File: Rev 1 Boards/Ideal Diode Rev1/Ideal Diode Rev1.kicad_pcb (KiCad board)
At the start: 2 copper layers, 66.8 x 54.6 mm, 21 parts, among them J2 Conn_01x02_Socket, J3 Conn_01x02_Socket, Q1 NVMFS5C404NL, U1 SN74LVC2G08, U2 LM74700

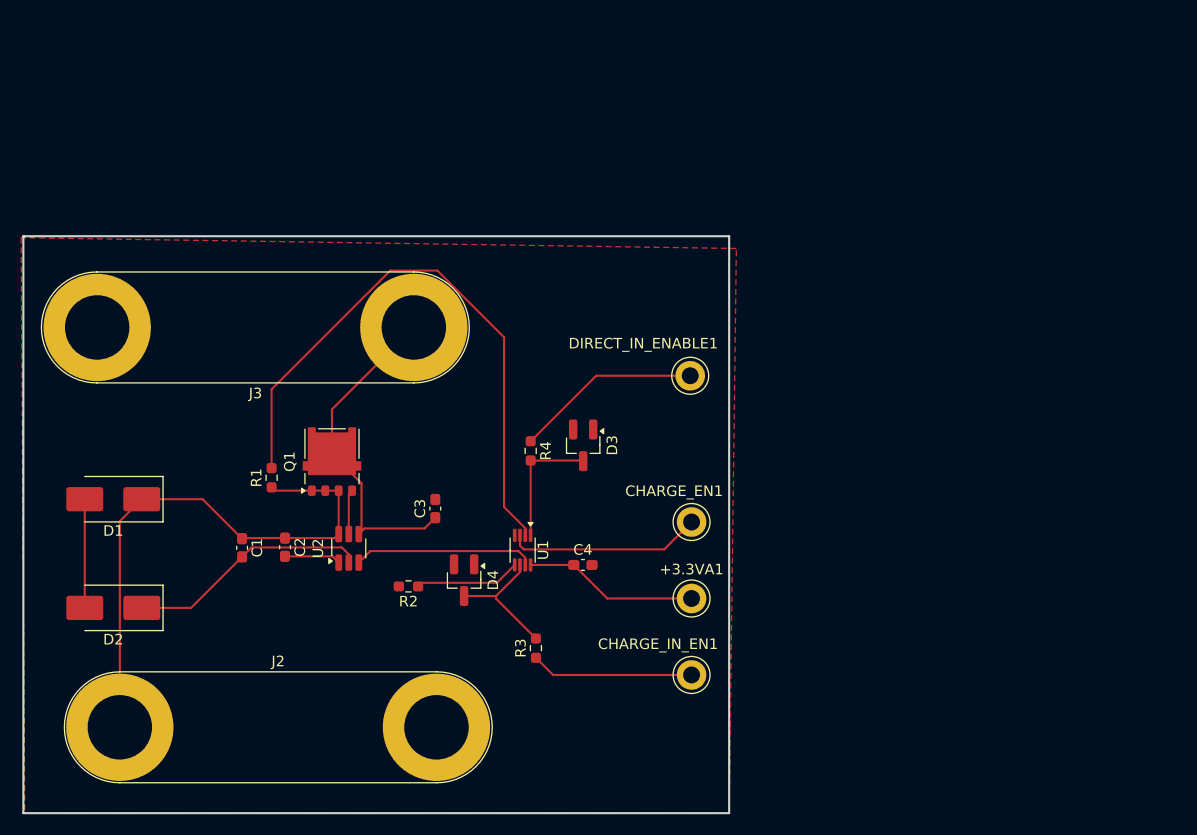
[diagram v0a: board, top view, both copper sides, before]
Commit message: finished ideal diode layout
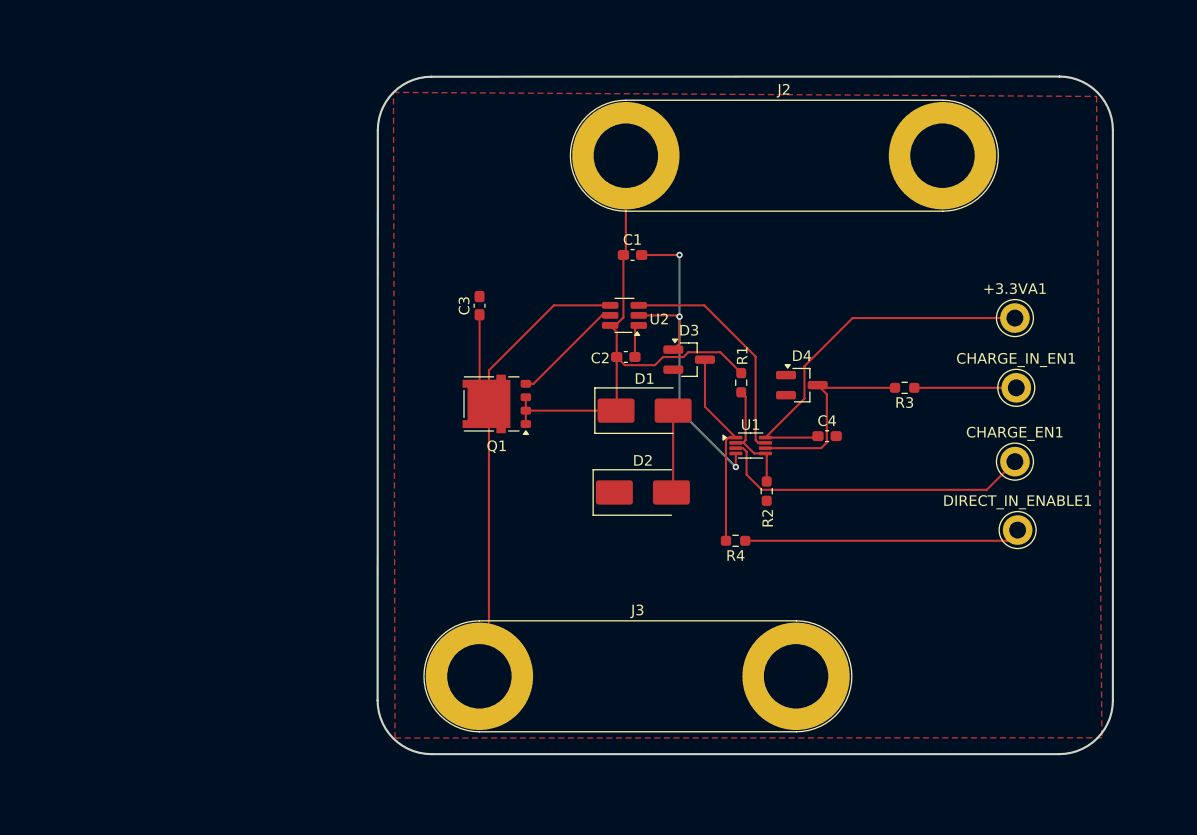
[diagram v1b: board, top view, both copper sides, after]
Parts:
- moved J2 72.3 mm to (85.3, 28.4)
- moved D2 51.3 mm to (87.0, 60.3), turned to 0 degrees
- moved D1 51.0 mm to (87.1, 52.6), turned to 0 degrees
- moved C1 46.2 mm to (86.0, 37.8), turned to 0 degrees
- moved R1 45.4 mm to (96.3, 49.9), turned to -90 degrees
- moved R3 42.7 mm to (111.7, 50.4), turned to 180 degrees
- moved CHARGE_IN_EN1 41.0 mm to (122.3, 50.4)
- moved +3.3VA1 40.5 mm to (122.2, 43.8)
- moved C2 36.9 mm to (85.3, 47.5), turned to 0 degrees
- moved D4 36.9 mm to (102.0, 50.2), turned to 0 degrees
- moved R2 35.1 mm to (98.7, 60.2), turned to -90 degrees
- moved DIRECT_IN_ENABLE1 34.3 mm to (122.4, 63.9)
- moved U2 34.2 mm to (85.2, 43.6), turned to 180 degrees
- moved J3 33.6 mm to (71.5, 77.7), turned to 0 degrees
- moved CHARGE_EN1 31.1 mm to (122.2, 57.4)
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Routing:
- net /Ideal Diode/V_{ON}: track 66.3 -> 11.7 mm
- net /Ideal Diode/OUT: track 31.9 -> 52.7 mm
- net +3.3VA: track 16.6 -> 35.1 mm
- net /Ideal Diode/CHARGING_EN: track 18.4 -> 30.4 mm
- net GNDPWR: track 23.0 -> 34.4 mm, vias 0 -> 3
- net /Ideal Diode/DIRECT_IEN: track 17.7 -> 26.2 mm
- net /Ideal Diode/D_CLIP: track 12.1 -> 19.1 mm
- net /Ideal Diode/C_CLIP: track 12.5 -> 19.2 mm
- net /Ideal Diode/GATE: track 4.24 -> 10.7 mm
- net /Ideal Diode/CHARGING_IEN: track 15.4 -> 9.65 mm
- net /Ideal Diode/DIRECT_EN: track 17.1 -> 22.0 mm
- net /Ideal Diode/IN: track 53.7 -> 51.2 mm
- net /Ideal Diode/TVS_mid: track 10.3 -> 7.81 mm
- net /Ideal Diode/VCAP: track 5.33 -> 3.14 mm
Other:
- board size 66.8 x 54.6 mm -> 69.6 x 64.1 mm

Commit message: ideal diode review 1 updates
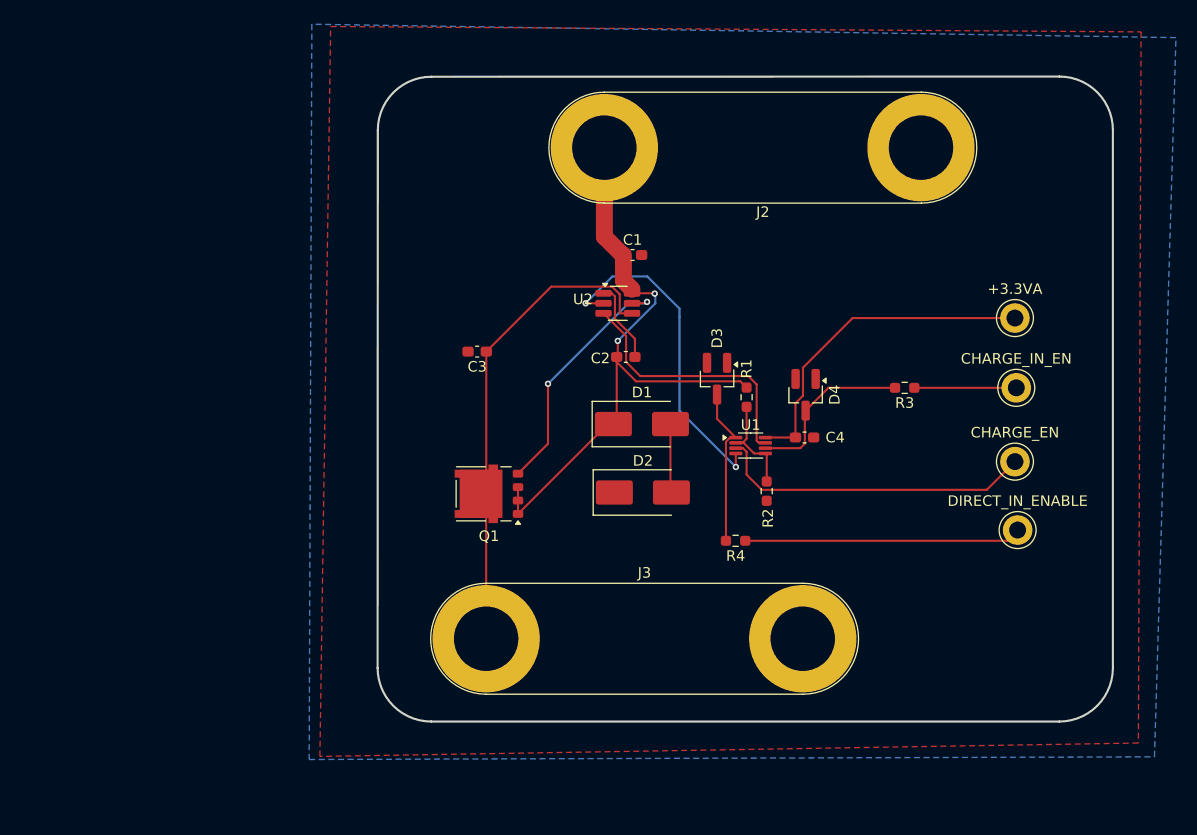
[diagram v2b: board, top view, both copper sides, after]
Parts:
- moved Q1 8.54 mm to (72.4, 60.5)
- moved C3 4.35 mm to (71.3, 47.0), turned to 180 degrees
- moved J3 3.61 mm to (72.1, 74.2)
- moved D3 3.20 mm to (94.0, 49.6), turned to -90 degrees
- moved J2 2.17 mm to (83.3, 27.7)
- moved C4 2.14 mm to (102.3, 55.1)
- moved R1 1.46 mm to (96.8, 51.3)
- moved U2 1.31 mm to (84.6, 42.4), turned to 0 degrees
- moved D1 1.30 mm to (86.9, 53.8)
- moved D4 0.98 mm to (102.4, 51.1), turned to -90 degrees
- renumbered +3.3VA1 to +3.3VA, CHARGE_EN1 to CHARGE_EN, CHARGE_IN_EN1 to CHARGE_IN_EN, DIRECT_IN_ENABLE1 to DIRECT_IN_ENABLE
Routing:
- net /Ideal Diode/GATE: track 10.7 -> 23.8 mm, vias 0 -> 2
- net /Ideal Diode/IN: track 51.2 -> 60.9 mm, vias 0 -> 2
- net /Ideal Diode/VCAP: track 3.14 -> 7.72 mm
- net /Ideal Diode/OUT: track 52.7 -> 48.7 mm
- net /Ideal Diode/D_CLIP: track 19.1 -> 15.3 mm
- net +3.3VA: track 35.1 -> 31.8 mm
- net GNDPWR: track 34.4 -> 31.4 mm, vias 3 -> 2
- net /Ideal Diode/DIRECT_EN: track 22.0 -> 25.0 mm
- net /Ideal Diode/C_CLIP: track 19.2 -> 16.4 mm
- net /Ideal Diode/TVS_mid: track 7.81 -> 6.74 mm
- net /Ideal Diode/V_{ON}: track 11.7 -> 10.8 mm
- added copper zone on B.Cu, net GNDPWR
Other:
- board size 69.6 x 64.1 mm -> 69.6 x 61.1 mm
- board text added: "Andrew Kwa :)"

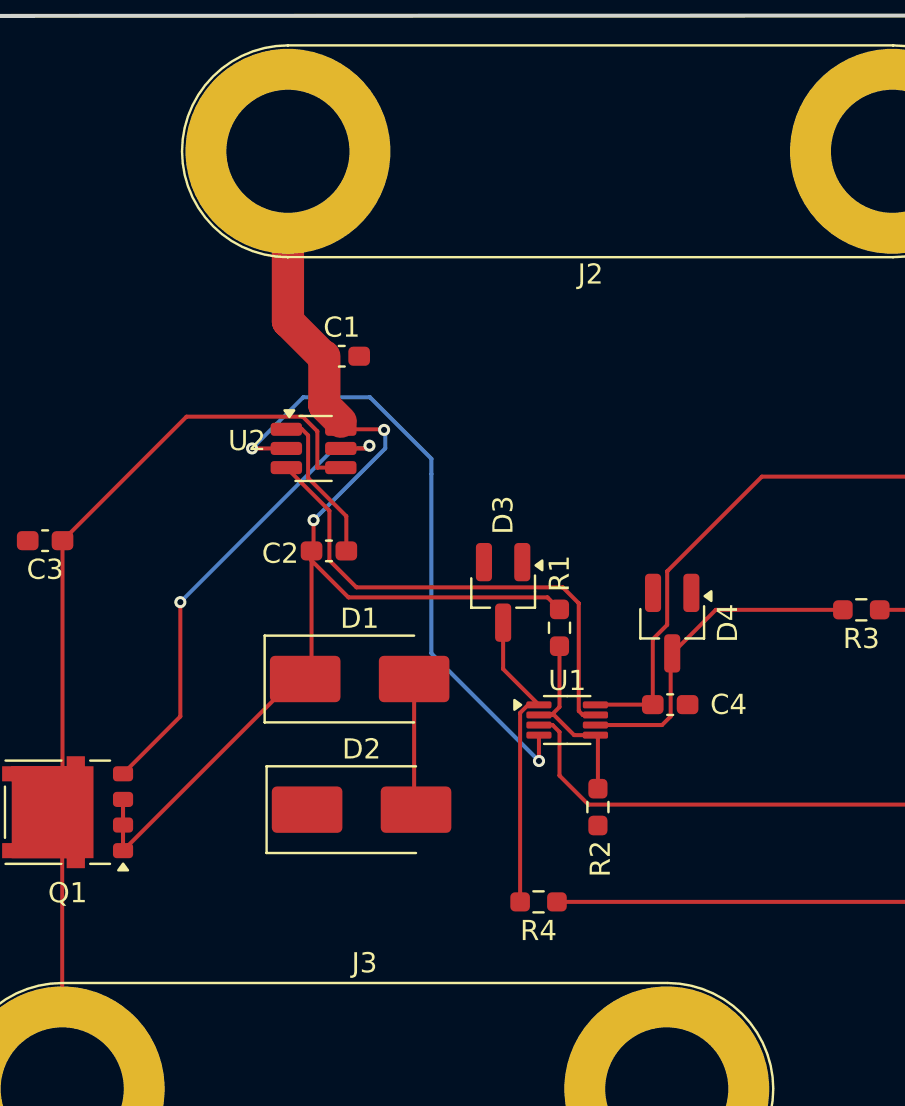
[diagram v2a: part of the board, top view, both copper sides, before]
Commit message: ideal diode review 1 changes
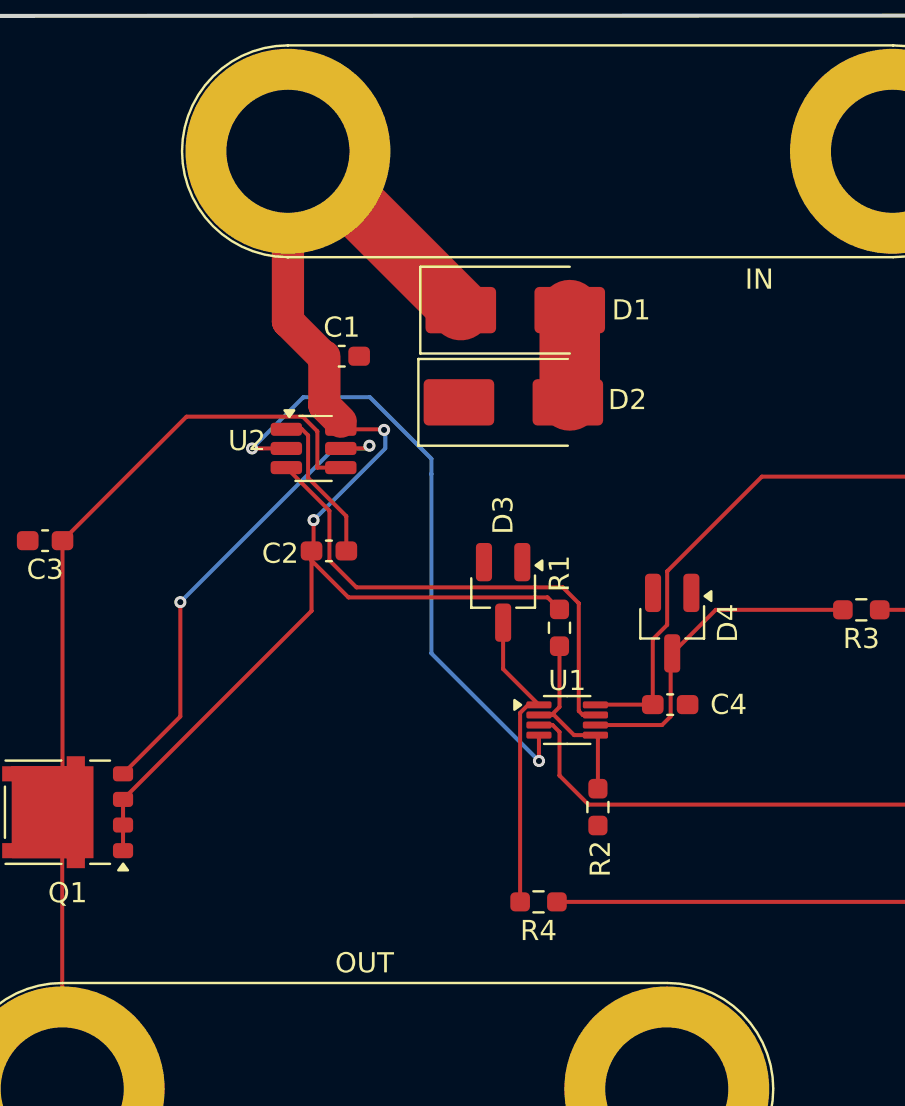
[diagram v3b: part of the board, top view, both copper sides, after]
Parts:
- added G***: LOGO, LOGO, B.Cu at (71.3, 32.2)
- moved D2 21.5 mm to (94.5, 40.1)
- moved D1 19.8 mm to (94.6, 35.6)
- renumbered J2 to IN, J3 to OUT
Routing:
- net /Ideal Diode/IN: track 60.9 -> 69.9 mm
- net /Ideal Diode/TVS_mid: track 6.74 -> 4.61 mm

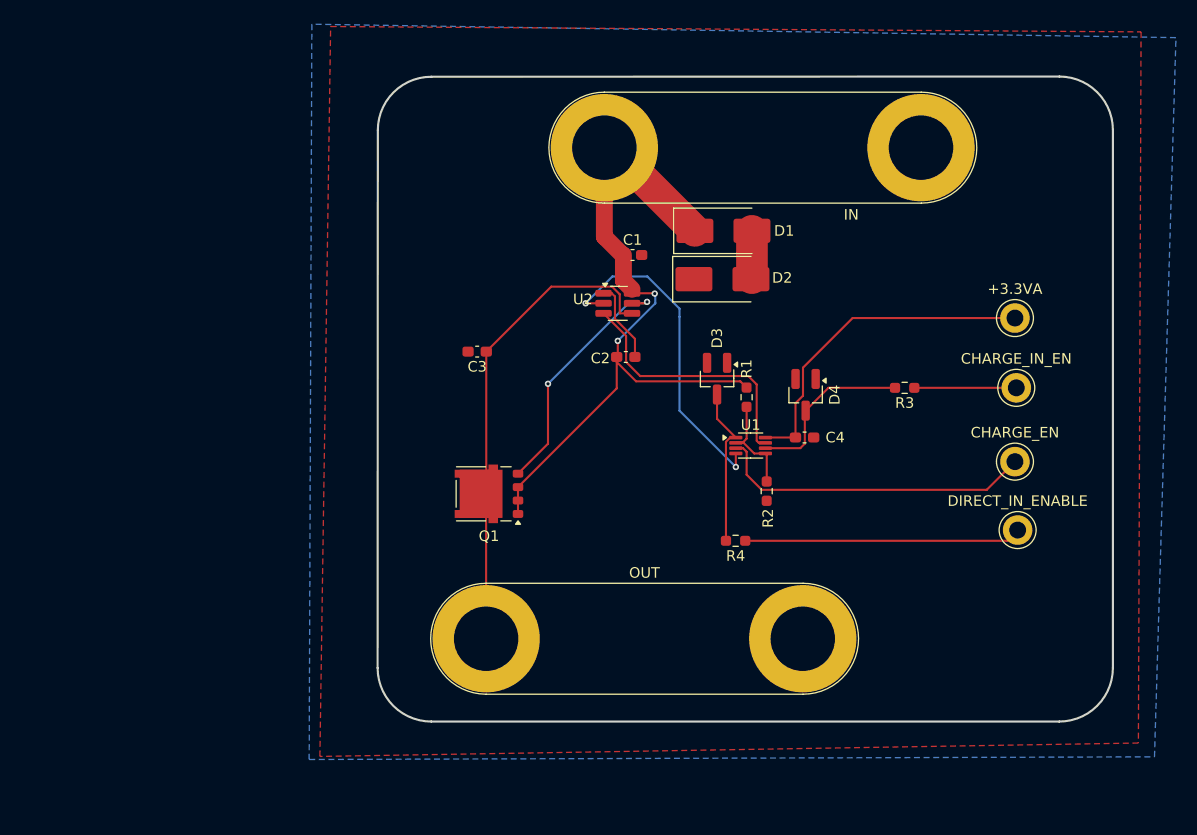
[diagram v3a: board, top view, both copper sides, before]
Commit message: review 1 ideal diode changes
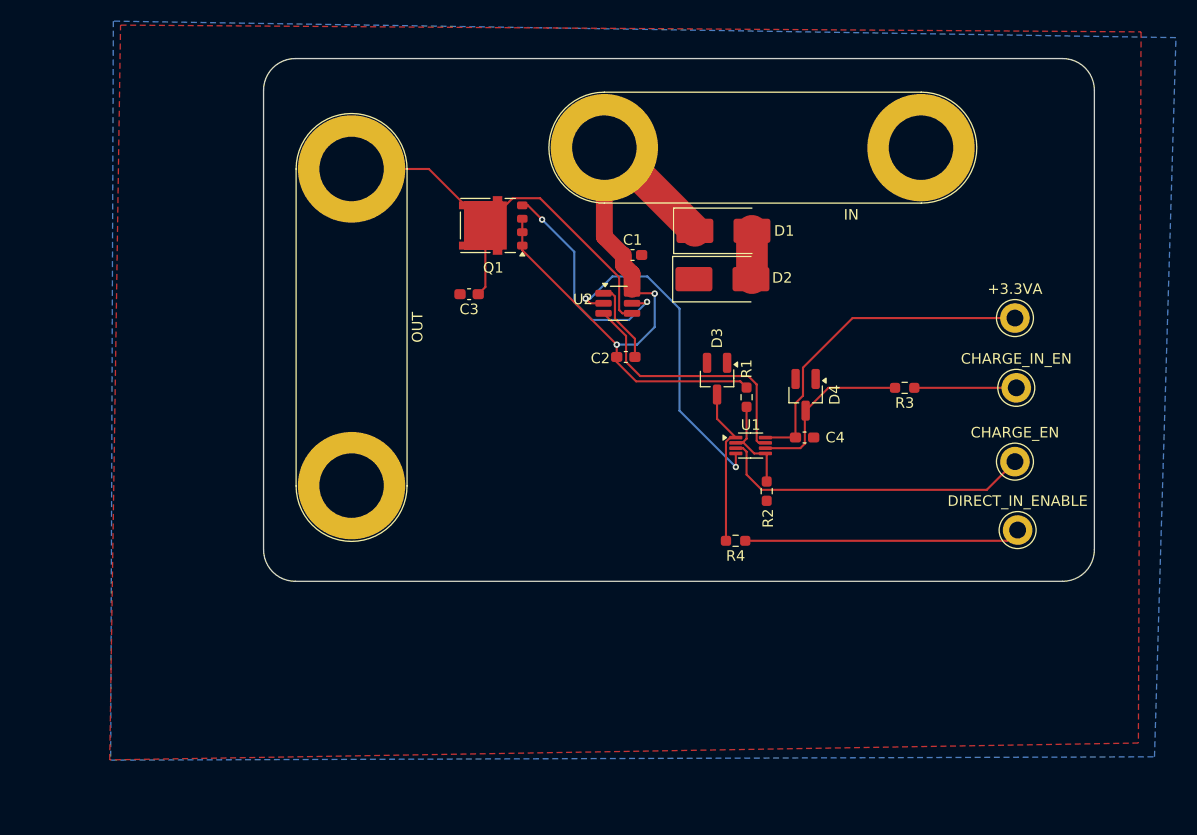
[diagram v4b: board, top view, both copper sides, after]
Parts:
- moved OUT 46.3 mm to (59.4, 29.7), turned to -90 degrees
- moved Q1 25.4 mm to (72.8, 35.1)
- moved G*** 19.8 mm to (76.5, 51.3)
- moved C3 5.49 mm to (70.5, 41.6)
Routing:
- net /Ideal Diode/OUT: track 48.7 -> 42.9 mm
- net /Ideal Diode/GATE: track 23.8 -> 21.5 mm
- net /Ideal Diode/IN: track 69.9 -> 68.0 mm
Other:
- board size 69.6 x 61.1 mm -> 78.6 x 49.5 mm

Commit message: ideal diode review 3 changes
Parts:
- moved IN 37.9 mm to (59.8, 57.5), turned to 90 degrees
- moved D1 30.5 mm to (73.2, 57.4)
- moved DIRECT_IN_ENABLE 25.9 mm to (96.6, 62.8)
- moved G*** 23.8 mm to (90.9, 32.4)
- moved D2 20.7 mm to (82.9, 57.4), turned to 180 degrees
- moved OUT 15.8 mm to (75.1, 31.7), turned to 0 degrees
- moved C1 15.2 mm to (81.8, 52.4), turned to 90 degrees
- moved +3.3VA 13.5 mm to (108.7, 43.8)
- moved CHARGE_IN_EN 13.3 mm to (109.0, 50.3)
- moved CHARGE_EN 13.2 mm to (109.0, 56.7)
- moved U2 13.0 mm to (74.4, 50.5), turned to 180 degrees
- moved C4 12.8 mm to (98.9, 42.8), turned to 90 degrees
- moved R3 12.4 mm to (99.5, 48.5)
- moved D4 12.0 mm to (92.8, 43.8)
- moved R1 10.8 mm to (86.0, 52.4), turned to 90 degrees
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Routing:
- net /Ideal Diode/IN: track 68.0 -> 40.1 mm, vias 2 -> 0
- net /Ideal Diode/DIRECT_IEN: track 26.2 -> 5.75 mm
- net GNDPWR: track 31.4 -> 11.5 mm
- net /Ideal Diode/OUT: track 42.9 -> 25.9 mm
- net /Ideal Diode/GATE: track 21.5 -> 4.91 mm, vias 2 -> 0
- net /Ideal Diode/CHARGING_EN: track 30.4 -> 18.8 mm
- net +3.3VA: track 31.8 -> 21.2 mm
- net /Ideal Diode/DIRECT_EN: track 25.0 -> 17.4 mm
- net /Ideal Diode/V_{ON}: track 10.8 -> 17.4 mm
- net /Ideal Diode/C_CLIP: track 16.4 -> 10.1 mm
- net /Ideal Diode/D_CLIP: track 15.3 -> 9.02 mm
- net /Ideal Diode/VCAP: track 7.72 -> 2.97 mm
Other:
- board size 78.6 x 49.5 mm -> 64.2 x 49.3 mm
